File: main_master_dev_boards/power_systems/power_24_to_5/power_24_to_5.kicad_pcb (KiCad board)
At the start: 2 copper layers, 71 x 30 mm, 31 parts, among them J1 Switch_in, J2 24_in, J3 GND_in, J4 PGoodMain_out, J5 ref_out, J6 5_out, J7 GND_out, J8 3v3_out, J9 PGoodBackup_out, U1 LMR16030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

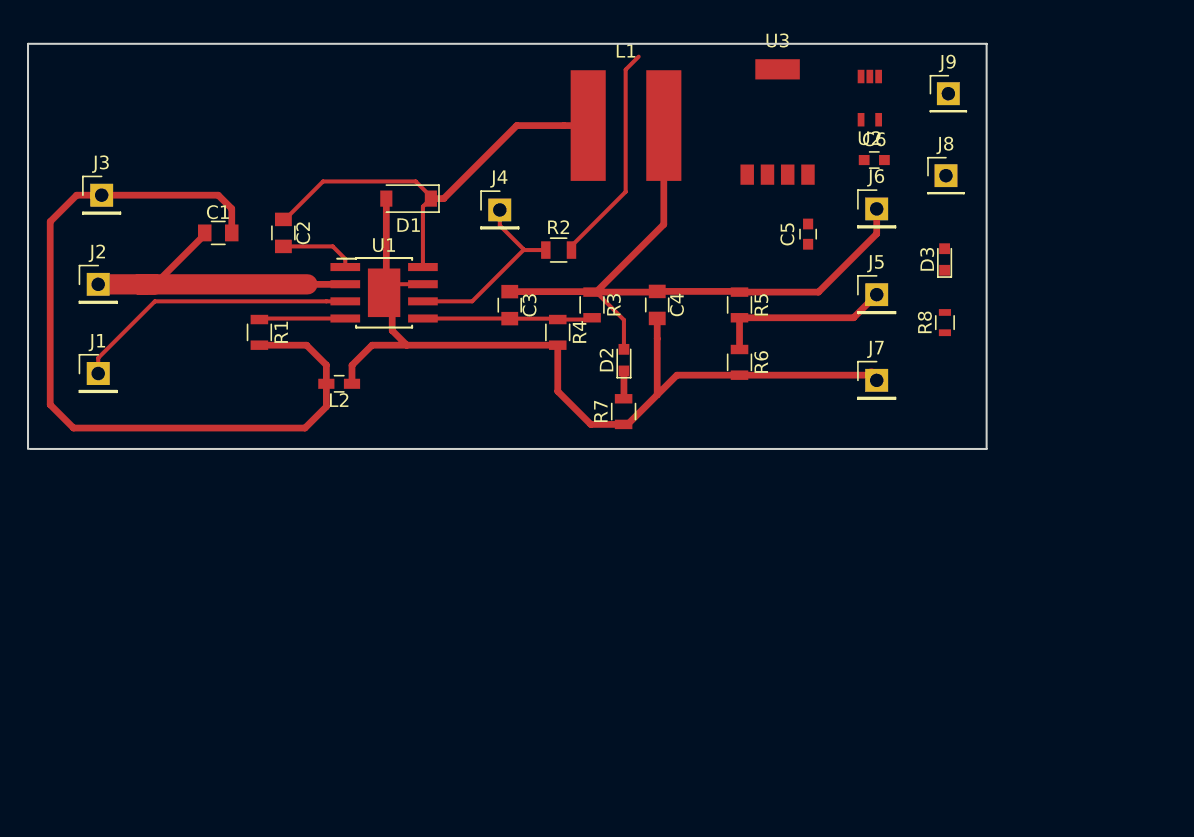
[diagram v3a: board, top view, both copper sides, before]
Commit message: Redesigned 24 to 5 dev board
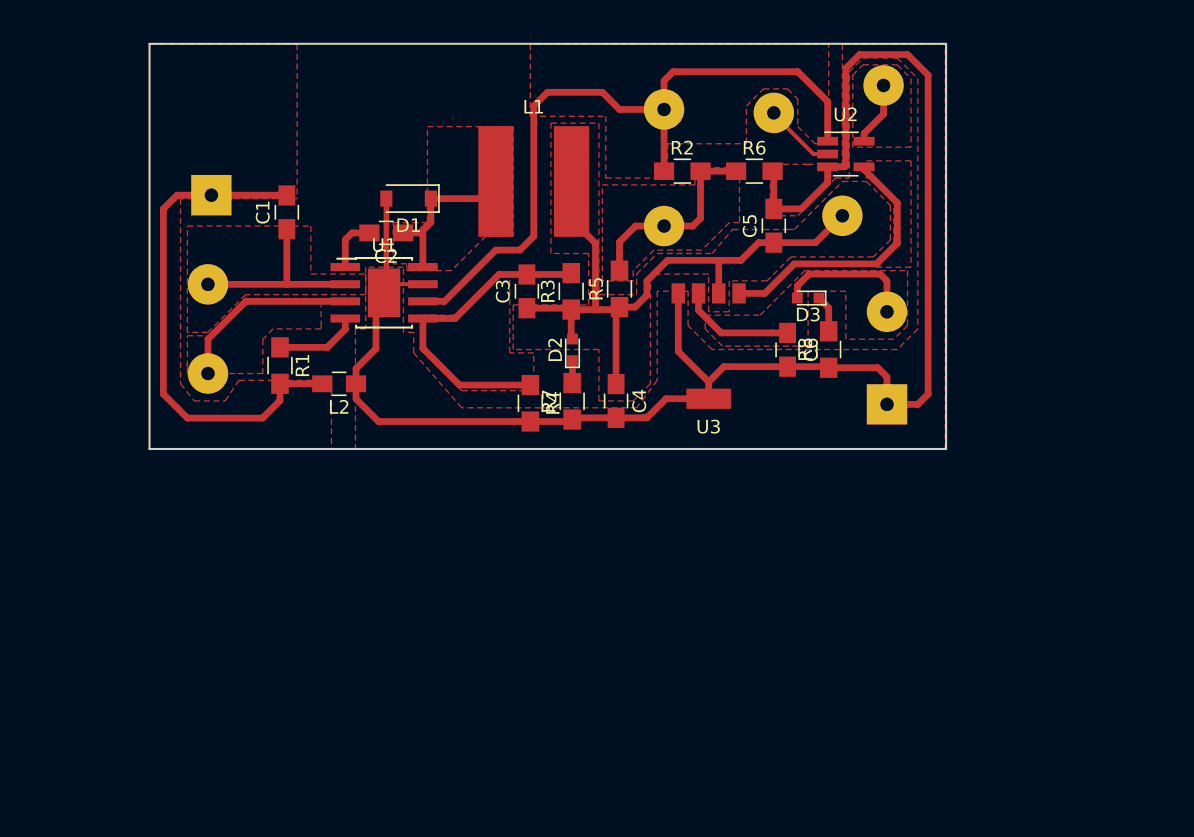
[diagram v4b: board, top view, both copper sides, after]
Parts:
- added J10: 5_in, pinheaders:pinhead-01x01_3x1, F.Cu at (134.4, 37.1)
- C1, C2, C3, C4: footprint Capacitors_SMD:C_0805 -> Capacitors_SMD:C_0805_HandSoldering
- C5, C6: footprint Capacitors_SMD:C_0603 -> Capacitors_SMD:C_0805_HandSoldering
- J1, J2, J4, J5, J6, J8, J9: footprint Pin_Headers:Pin_Header_Straight_1x01_Pitch2.54mm -> pinheaders:pinhead-01x01_3x1
- J3, J7: footprint Pin_Headers:Pin_Header_Straight_1x01_Pitch2.54mm -> pinheaders:pinhead-01x01_3x1_square
- L2: footprint Capacitors_SMD:C_0603_HandSoldering -> Capacitors_SMD:C_0805_HandSoldering
- R1, R2, R3, R4, R5, R6, R7: footprint Resistors_SMD:R_0805 -> Resistors_SMD:R_0805_HandSoldering
- R8: footprint Resistors_SMD:R_0603 -> Resistors_SMD:R_0805_HandSoldering
- U2: footprint SO-70:SO-70 -> TO_SOT_Packages_SMD:SOT-23-5_HandSoldering
- moved U3 17.4 mm to (121.4, 56.4), turned to 180 degrees
- moved J5 16.5 mm to (118.1, 47.5)
- moved C6 15.5 mm to (127.3, 56.7), turned to 270 degrees
- moved J4 14.3 mm to (118.1, 38.9)
- moved R6 14.2 mm to (124.8, 43.4), turned to 0 degrees
- moved J9 13.0 mm to (126.2, 39.1)
- moved J8 11.0 mm to (134.6, 53.8)
- moved R2 10.9 mm to (119.5, 43.4)
- moved D3 10.5 mm to (128.8, 52.8), turned to 180 degrees
- moved R5 8.97 mm to (114.8, 52.1), turned to 90 degrees
- moved R8 8.84 mm to (130.3, 56.6)
- moved J1 8.13 mm to (84.3, 58.4)
- moved J2 8.13 mm to (84.3, 51.8)
- moved J3 8.13 mm to (84.6, 45.2)
- moved L1 7.99 mm to (108.5, 44.2)
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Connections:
- D2 pad 2: Net-(D2-Pad2) -> /V5_MAIN
- R7 pad 2: Net-(R7-Pad2) -> Net-(D2-Pad1)
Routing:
- net GND: track 69.4 -> 125.1 mm
- net /PG_v5_main: track 14.4 -> 53.4 mm
- net /GND24: track 60.5 -> 37.6 mm
- net /v5_good: track 0.00 -> 19.9 mm
- net /3V3_out: track 0.00 -> 18.9 mm
- net Net-(C2-Pad1): track 31.9 -> 13.2 mm
- net /P_ref_buc: track 29.6 -> 15.0 mm
- net Net-(C3-Pad2): track 12.6 -> 23.7 mm
- net /V24: track 25.0 -> 14.3 mm
- net /Switch_on: track 21.2 -> 13.9 mm
- net /PG_v5_backup: track 0.00 -> 5.31 mm
- net VCC: track 0.00 -> 4.73 mm
- net Net-(D3-Pad1): track 0.00 -> 2.76 mm
- net Net-(D2-Pad2): track 2.18 -> 0.00 mm
- net Net-(R7-Pad2): track 2.07 -> 0.00 mm
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- added copper zone on F.Cu, net /3V3_out
- added copper zone on F.Cu, net /GND24
- added copper zone on F.Cu, net /PG_v5_main
- added copper zone on F.Cu, net /P_ref_buc
- added copper zone on F.Cu, net /Switch_on
- added copper zone on F.Cu, net /V24
- added copper zone on F.Cu, net /V5_MAIN
- added copper zone on F.Cu, net /v5_good
- added copper zone on F.Cu, net GND
- added copper zone on F.Cu, net Net-(C2-Pad1)
- added copper zone on F.Cu, net Net-(C3-Pad2)
- added copper zone on F.Cu, net VCC
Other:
- board size 71 x 30 mm -> 59 x 30 mm
- rule trace_min: 0.2 -> 0.25

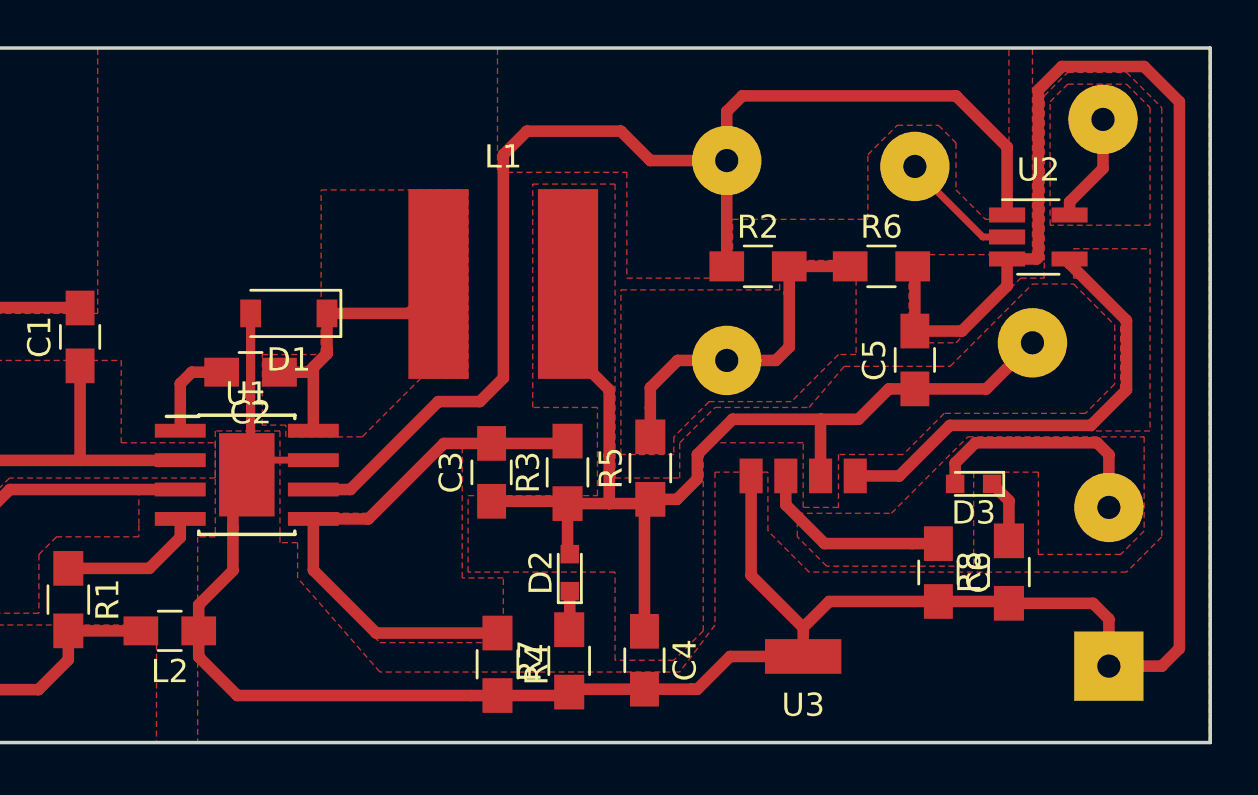
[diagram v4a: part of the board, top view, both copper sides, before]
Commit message: refined the two dev boards 24_to_5 and power_switch
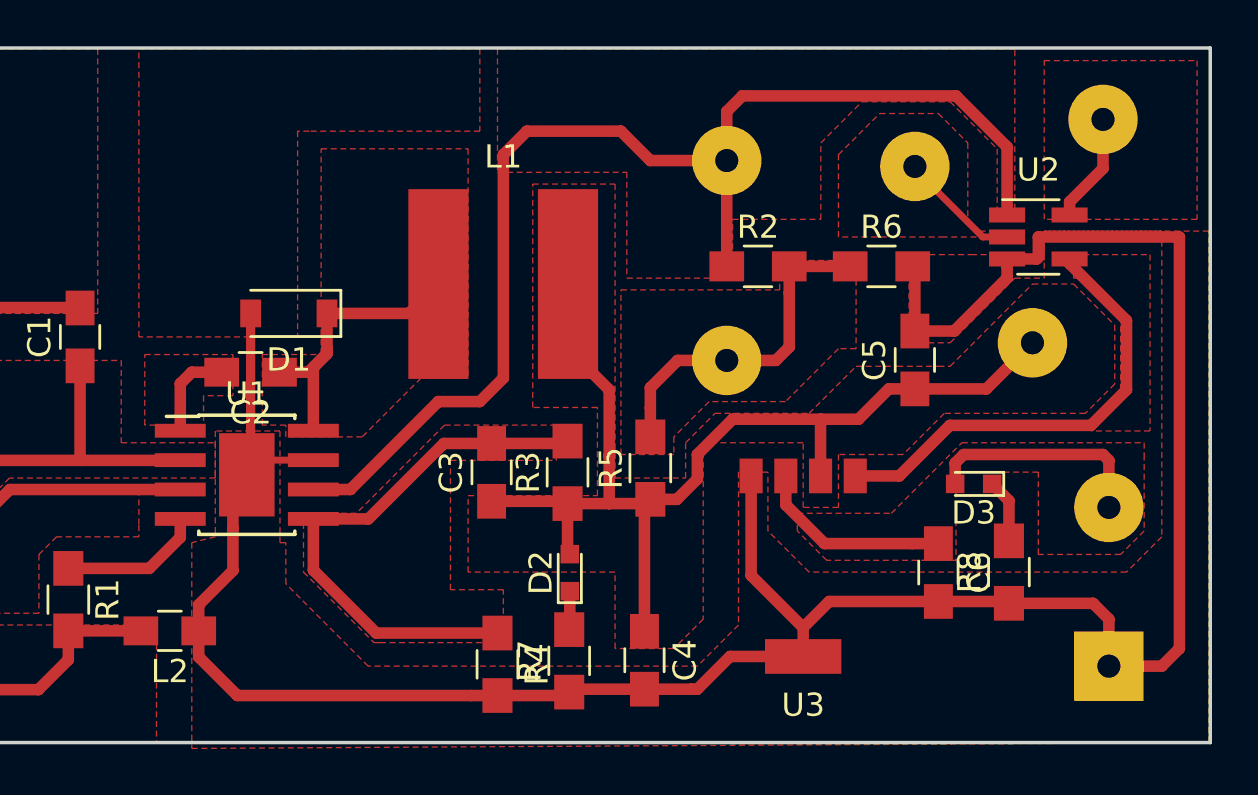
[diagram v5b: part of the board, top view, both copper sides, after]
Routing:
- net GND: track 125.1 -> 111.6 mm
- net /3V3_out: track 18.9 -> 18.4 mm
- added copper zone on F.Cu, net /PG_v5_backup
- added copper zone on F.Cu, net Net-(C2-Pad2)

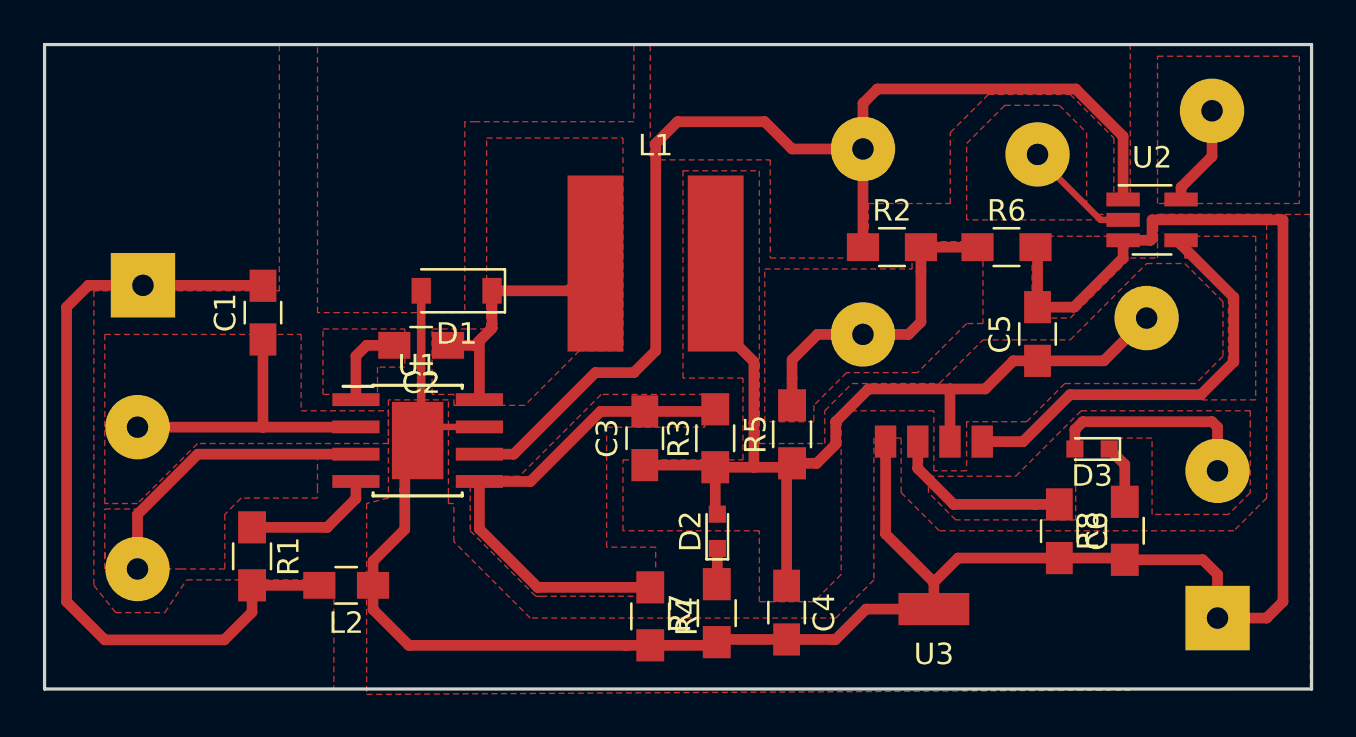
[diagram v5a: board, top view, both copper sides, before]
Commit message: Created new branch and modified 24 to 5 buck with values from datasheet
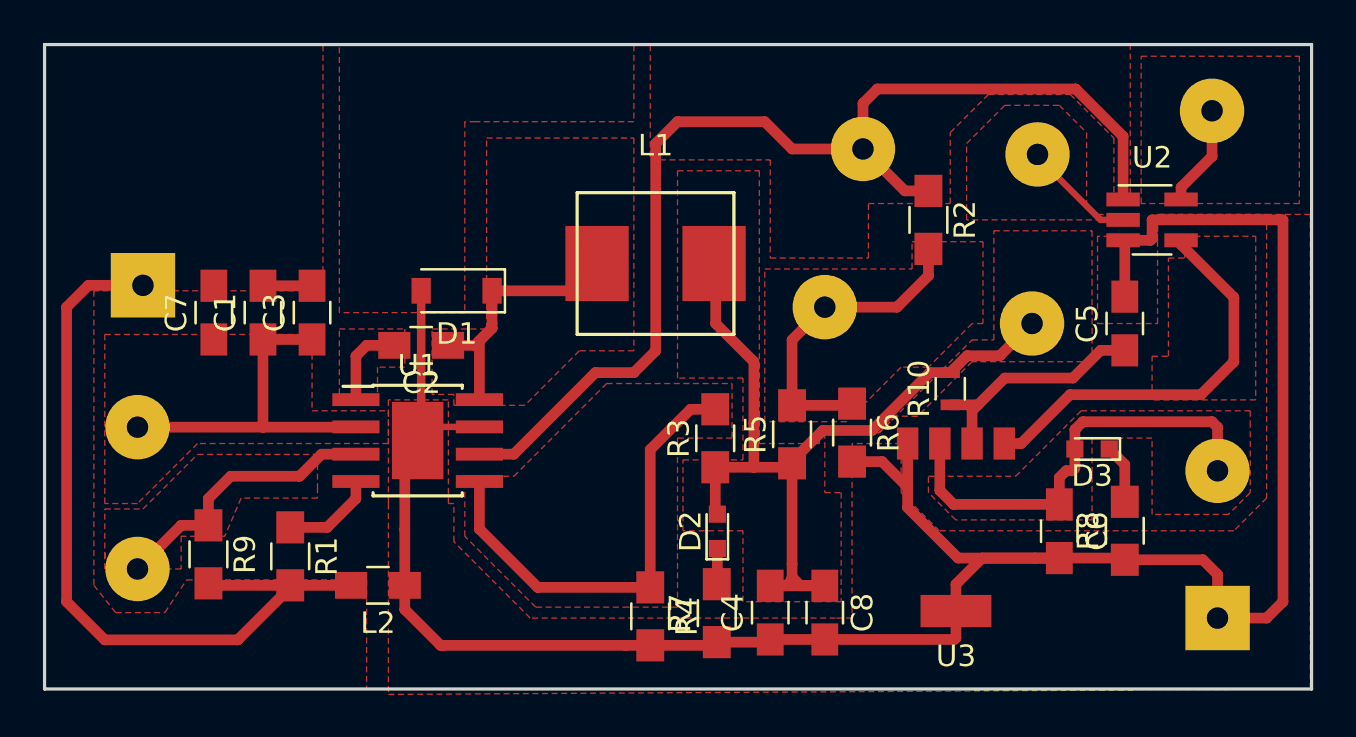
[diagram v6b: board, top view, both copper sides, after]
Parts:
- added C7: 0.1uF, Capacitors_SMD:C_0805_HandSoldering, F.Cu at (87.9, 46.5)
- added C8: 47uF X7R, Capacitors_SMD:C_0805_HandSoldering, F.Cu at (116.3, 60.5)
- added R10: 0, Resistors_SMD:R_0603, F.Cu at (122.2, 50.0)
- added R9: 10K, Resistors_SMD:R_0805_HandSoldering, F.Cu at (87.6, 57.7)
- C3: value 27pF -> 2.2uF
- C4: value 33uF -> 47uF X7R
- C5, C6: value 22uF -> 10uF
- L1: value 15uH -> 8.2uH; footprint Bourns:Bourns-8040 -> Bourns:Bourns-SRP7028A
- R1: value 45.3K -> 49.9K
- R3: value 68K -> 100K
- R4: value 12K -> 17.8K
- R8: value 10 -> 100
- moved C3 16.6 mm to (92.5, 46.5)
- moved R6 11.2 mm to (117.6, 52.1), turned to 270 degrees
- moved J6 5.34 mm to (126.0, 47.0)
- moved C5 4.09 mm to (130.3, 47.0)
- moved J5 2.18 mm to (116.3, 46.2)
- moved R2 2.12 mm to (121.2, 42.2), turned to 270 degrees
- moved R1 1.78 mm to (91.4, 57.8)
- moved L2 1.48 mm to (95.5, 59.2)
- moved U3 1.03 mm to (122.4, 56.5)
- moved C4 0.76 mm to (113.8, 60.5), turned to 90 degrees
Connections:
- C3 pad 1: /V5_MAIN -> /V24
- C3 pad 2: Net-(C3-Pad2) -> /GND24
- C4 pad 1: /V5_MAIN -> GND
- C4 pad 2: GND -> /V5_MAIN
- C5 pad 1: /V5_MAIN -> Net-(C5-Pad1)
- R3 pad 2: Net-(C3-Pad2) -> Net-(R3-Pad2)
- R4 pad 1: Net-(C3-Pad2) -> Net-(R3-Pad2)
- U1 pad 5: Net-(C3-Pad2) -> Net-(R3-Pad2)
- U3 pad 2: /V5_MAIN -> Net-(C5-Pad1)
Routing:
- net Net-(C3-Pad2): track 23.7 -> 0.00 mm
- net Net-(R3-Pad2): track 0.00 -> 21.7 mm
- net Net-(C5-Pad1): track 0.00 -> 11.1 mm
- net /V5_MAIN: track 47.6 -> 41.0 mm
- net /3V3_out: track 18.4 -> 20.9 mm
- net /V24: track 14.3 -> 16.5 mm
- net Net-(R1-Pad1): track 6.19 -> 4.41 mm
- net /GND24: track 37.6 -> 39.0 mm
- net /v5_good: track 19.9 -> 18.9 mm
- net /Switch_on: track 13.9 -> 13.1 mm
- net /PG_v5_main: track 53.4 -> 52.7 mm
- added copper zone on F.Cu, net Net-(R3-Pad2)
- removed copper zone on F.Cu, net Net-(C3-Pad2)

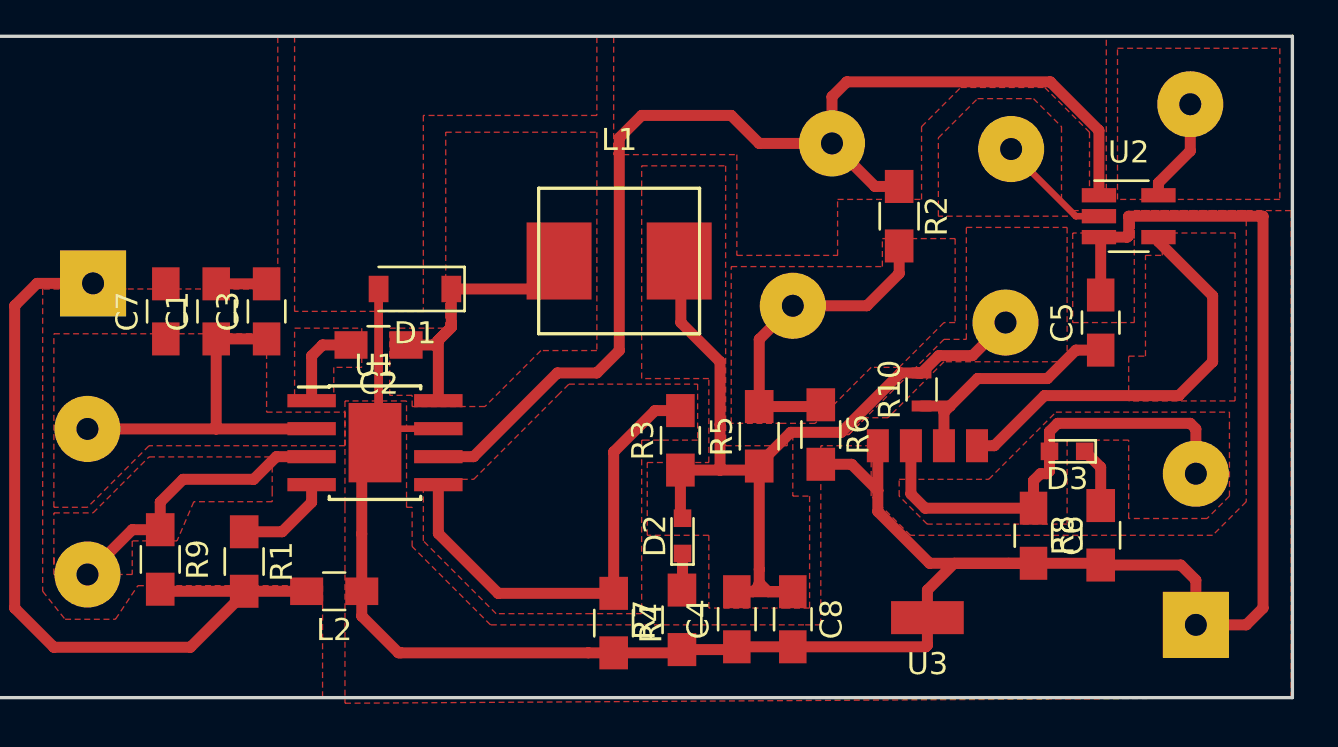
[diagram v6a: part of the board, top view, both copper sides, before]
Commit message: Added correct caps for buck and LDO. Changed the or gate to 5V tollerant variant
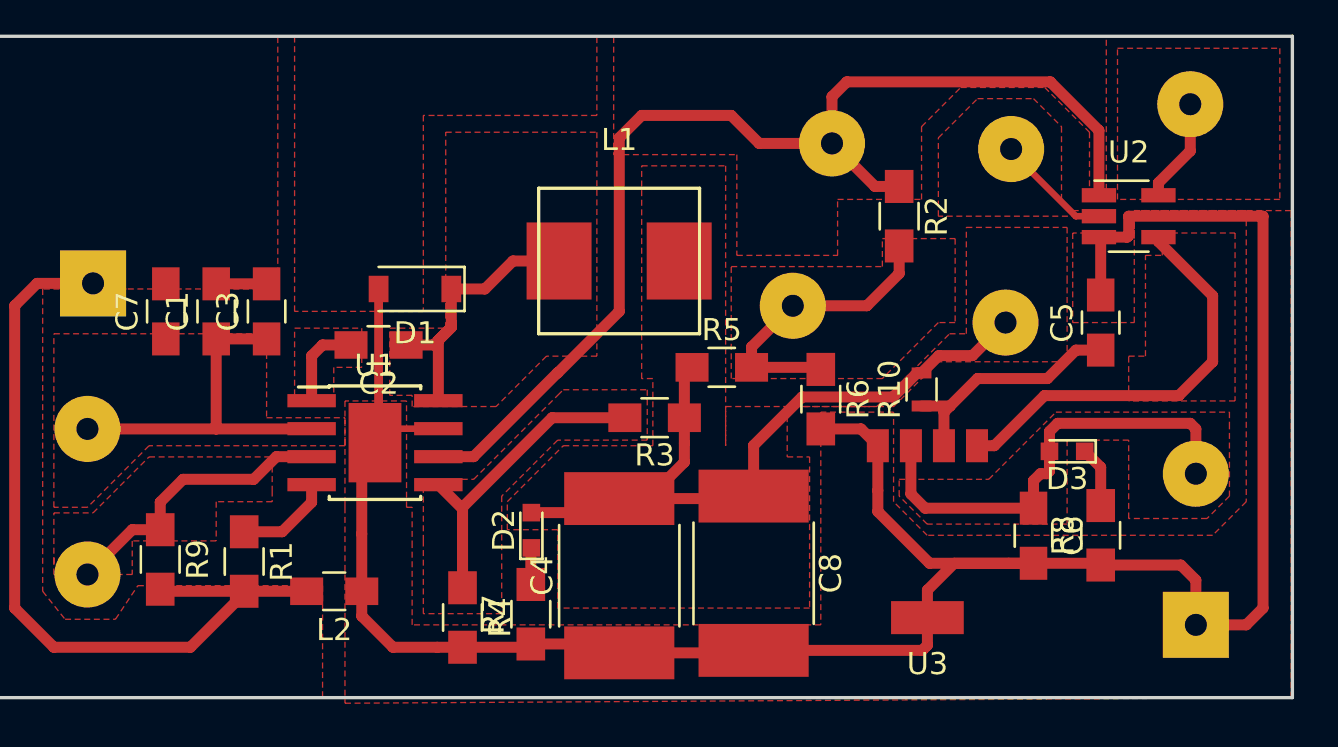
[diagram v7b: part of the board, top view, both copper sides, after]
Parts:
- C4, C8: footprint Capacitors_SMD:C_0805_HandSoldering -> Capacitors_SMD:C_2220_HandSoldering
- U2: value 74AUC1G32 -> MC74HC1G32DTT1G
- moved R7 6.86 mm to (104.4, 60.2)
- moved D2 6.86 mm to (104.5, 56.4)
- moved R4 6.86 mm to (101.3, 60.4)
- moved C4 5.69 mm to (108.5, 58.5)
- moved R5 3.56 mm to (113.1, 49.0), turned to 0 degrees
- moved C8 2.74 mm to (114.6, 58.4)
- moved R6 1.60 mm to (117.6, 50.5)
- moved R3 1.56 mm to (110.1, 51.3), turned to 180 degrees
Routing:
- net /V5_MAIN: track 41.0 -> 34.5 mm
- net Net-(R3-Pad2): track 21.7 -> 17.8 mm
- net /P_ref_buc: track 14.7 -> 13.4 mm
- net /PG_v5_main: track 52.7 -> 51.6 mm
